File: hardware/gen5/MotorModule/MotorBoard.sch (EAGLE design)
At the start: 39 parts, among them J1 M20X2SHROUDED

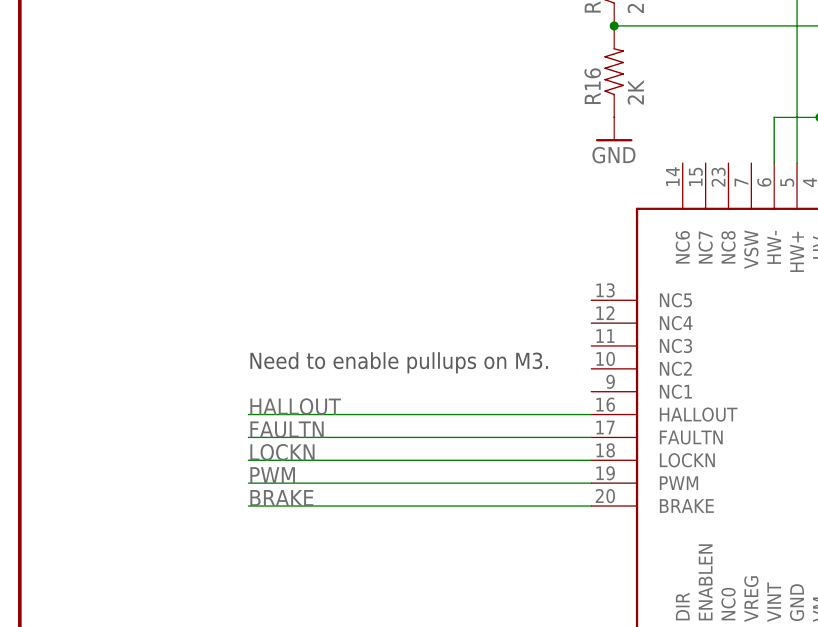
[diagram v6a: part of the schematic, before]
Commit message: added pullups to the motorboard, and did DRC checking
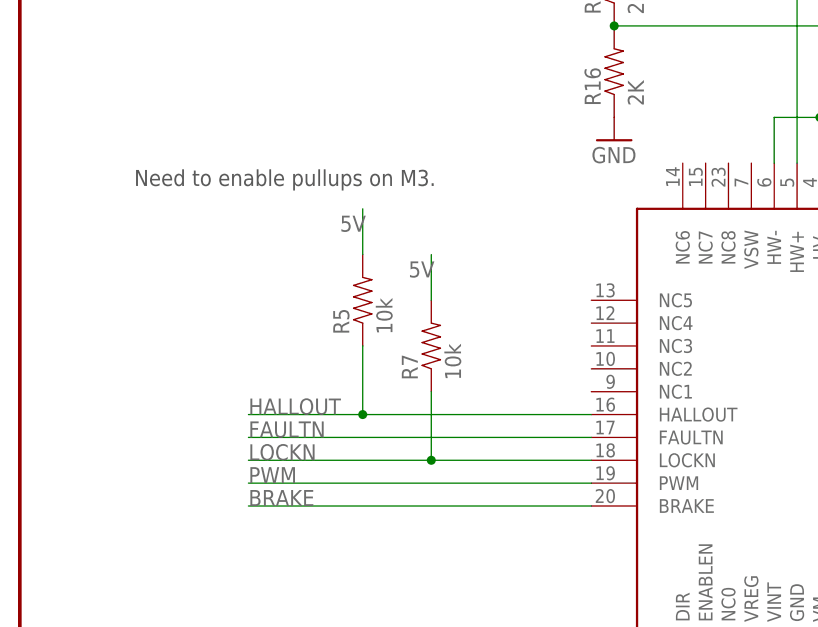
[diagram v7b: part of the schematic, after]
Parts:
- added R5, R7: 10k, SparkFun-Resistors:RESISTOR0805-RES
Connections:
- net 5V: now also R5.2, R7.2
- net HALLOUT: now also R5.1
- net LOCKN: now also R7.1
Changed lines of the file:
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@@
 <?xml version="1.0" encoding="utf-8"?>
 <!DOCTYPE eagle SYSTEM "eagle.dtd">
-<eagle version="7.2.0">
+<eagle version="7.4.0">
 <drawing>
 <settings>
@@
 <part name="GND8" library="SparkFun-Aesthetics" deviceset="GND" device=""/>
 <part name="GND9" library="SparkFun-Aesthetics" deviceset="GND" device=""/>
+<part name="R5" library="SparkFun-Resistors" deviceset="RESISTOR" device="0805-RES" value="10k"/>
+<part name="R7" library="SparkFun-Resistors" deviceset="RESISTOR" device="0805-RES" value="10k"/>
 </parts>
 <sheets>
@@
 <text x="157.48" y="53.34" size="1.778" layer="97">Separate connector?</text>
 <text x="254" y="81.28" size="1.778" layer="97">24, 26, and 30 are unconnected in Rev A</text>
-<text x="25.4" y="71.12" size="1.778" layer="97">Need to enable pullups on M3.</text>
+<text x="12.7" y="91.44" size="1.778" layer="97">Need to enable pullups on M3.</text>
 </plain>
 <instances>
@@
 <instance part="GND8" gate="1" x="139.7" y="2.54"/>
 <instance part="GND9" gate="1" x="213.36" y="60.96"/>
+<instance part="R5" gate="G$1" x="38.1" y="78.74" rot="R90"/>
+<instance part="R7" gate="G$1" x="45.72" y="73.66" rot="R90"/>
 </instances>
 <busses>
@@
 <segment>
 <pinref part="U$1" gate="G$1" pin="HALLOUT"/>
-<wire x1="63.5" y1="66.04" x2="25.4" y2="66.04" width="0.1524" layer="91"/>
+<wire x1="63.5" y1="66.04" x2="38.1" y2="66.04" width="0.1524" layer="91"/>
 <label x="25.4" y="66.04" size="1.778" layer="95"/>
+<pinref part="R5" gate="G$1" pin="1"/>
+<wire x1="38.1" y1="66.04" x2="25.4" y2="66.04" width="0.1524" layer="91"/>
+<wire x1="38.1" y1="73.66" x2="38.1" y2="66.04" width="0.1524" layer="91"/>
+<junction x="38.1" y="66.04"/>
 </segment>
 <segment>
@@
 <wire x1="215.9" y1="139.7" x2="215.9" y2="142.24" width="0.1524" layer="91"/>
 </segment>
+<segment>
+<pinref part="R5" gate="G$1" pin="2"/>
+<wire x1="38.1" y1="83.82" x2="38.1" y2="88.9" width="0.1524" layer="91"/>
+<label x="35.56" y="86.36" size="1.778" layer="95"/>
+</segment>
+<segment>
+<pinref part="R7" gate="G$1" pin="2"/>
+<wire x1="45.72" y1="78.74" x2="45.72" y2="83.82" width="0.1524" layer="91"/>
+<label x="43.18" y="81.28" size="1.778" layer="95"/>
+</segment>
 </net>
 <net name="LOCKN" class="0">
 <segment>
 <pinref part="U$1" gate="G$1" pin="LOCKN"/>
-<wire x1="25.4" y1="60.96" x2="63.5" y2="60.96" width="0.1524" layer="91"/>
+<wire x1="25.4" y1="60.96" x2="45.72" y2="60.96" width="0.1524" layer="91"/>
 <label x="25.4" y="60.96" size="1.778" layer="95"/>
-</segment>
-<segment>
+<pinref part="R7" gate="G$1" pin="1"/>
+<wire x1="45.72" y1="60.96" x2="63.5" y2="60.96" width="0.1524" layer="91"/>
+<wire x1="45.72" y1="68.58" x2="45.72" y2="60.96" width="0.1524" layer="91"/>
+<junction x="45.72" y="60.96"/>
+</segment>
+<segment>

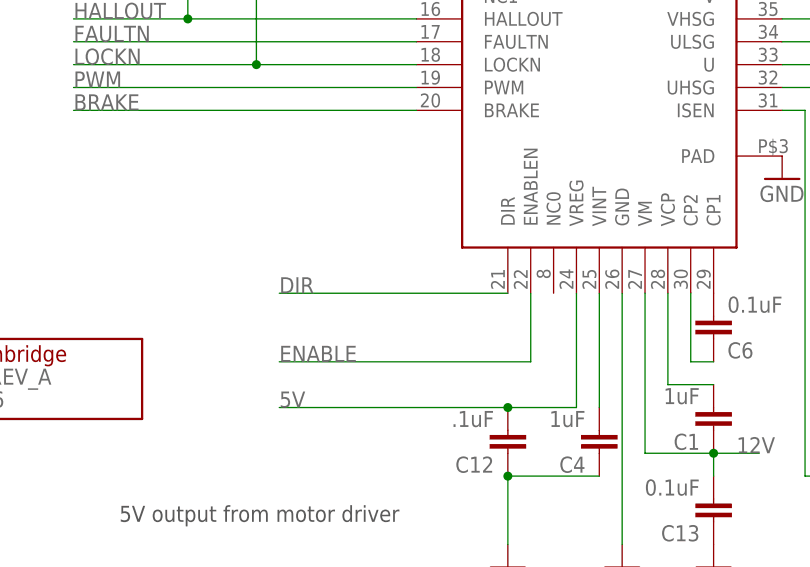
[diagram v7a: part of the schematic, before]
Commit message: added motorboard gerbers, but noticed some potential issues with grounding afterwards. Checking into it now. It appears that the commsboard is ready to go, however
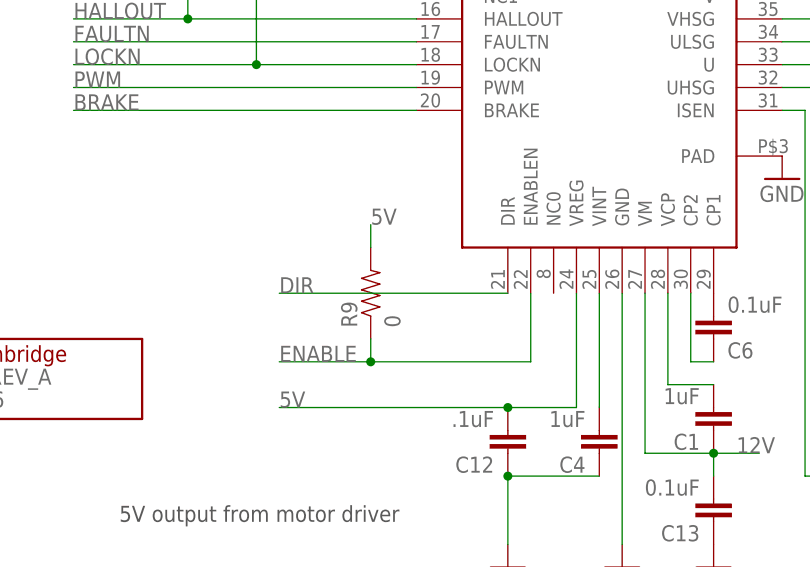
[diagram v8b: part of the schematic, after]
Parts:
- added R9: 0, SparkFun-Resistors:RESISTOR0805-RES
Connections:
- net 5V: now also R9.2
- net ENABLE: now also R9.1
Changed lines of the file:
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@@
 <part name="R5" library="SparkFun-Resistors" deviceset="RESISTOR" device="0805-RES" value="10k"/>
 <part name="R7" library="SparkFun-Resistors" deviceset="RESISTOR" device="0805-RES" value="10k"/>
+<part name="R9" library="SparkFun-Resistors" deviceset="RESISTOR" device="0805-RES" value="0"/>
 </parts>
 <sheets>
@@
 <instance part="R5" gate="G$1" x="38.1" y="78.74" rot="R90"/>
 <instance part="R7" gate="G$1" x="45.72" y="73.66" rot="R90"/>
+<instance part="R9" gate="G$1" x="58.42" y="35.56" rot="R90"/>
 </instances>
 <busses>
@@
 <net name="ENABLE" class="0">
 <segment>
-<wire x1="76.2" y1="27.94" x2="48.26" y2="27.94" width="0.1524" layer="91"/>
+<wire x1="76.2" y1="27.94" x2="58.42" y2="27.94" width="0.1524" layer="91"/>
 <label x="48.26" y="27.94" size="1.778" layer="95"/>
 <pinref part="U$1" gate="G$1" pin="ENABLEN"/>
+<wire x1="58.42" y1="27.94" x2="48.26" y2="27.94" width="0.1524" layer="91"/>
 <wire x1="76.2" y1="35.56" x2="76.2" y2="27.94" width="0.1524" layer="91"/>
+<pinref part="R9" gate="G$1" pin="1"/>
+<wire x1="58.42" y1="27.94" x2="58.42" y2="30.48" width="0.1524" layer="91"/>
+<junction x="58.42" y="27.94"/>
 </segment>
 <segment>
@@
 <label x="43.18" y="81.28" size="1.778" layer="95"/>
 </segment>
-</net>
+<segment>
+<pinref part="R9" gate="G$1" pin="2"/>
+<wire x1="58.42" y1="40.64" x2="58.42" y2="43.18" width="0.1524" layer="91"/>
+<label x="58.42" y="43.18" size="1.778" layer="95"/>
+</segment>
+</net>
